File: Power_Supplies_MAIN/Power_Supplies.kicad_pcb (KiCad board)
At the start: 4 copper layers, 343.1 x 201.9 mm, 229 parts, among them IC1 PCM1865DBT, IC2 LM2940IMPX-10_NOPB, IC3 XC6902NA01PR-G, IC5 PCM1865DBT, J1 Line Out (Left), J10 XLR3_AudioJack3_Combo, J11 PINHD_1x4_Female, J13 PINHD_1x10_Female, J14 PINHD_1x10_Female, J2 Headphone Out, J20 ACJM-MV-2, J21 Line Out (Right), J29 PINHD_1x2_Female, J3 XLR3_AudioJack3_Combo, J30 PINHD_1x2_Female, J31 PINHD_1x2_Female, J32 PINHD_1x2_Female, J33 PINHD_1x3_Female, J36 PINHD_1x2_Female, J4 XLR3_AudioJack3_Combo, J5 ACJM-MV-2, J6 ACJM-MV-2, J7 ACJM-MV-2, J9 XLR3_AudioJack3_Combo, U10 OPA2134, U11 TPA6110A2DGN, U15 OPA2134, U16 SSM2019BRNZ, U17 SSM2019BRNZ, U18 OPA2134, U19 SSM2019BRNZ, U20 SSM2019BRNZ, U34 NE5532AD, U35 NE5532AD, U9 PCM1780

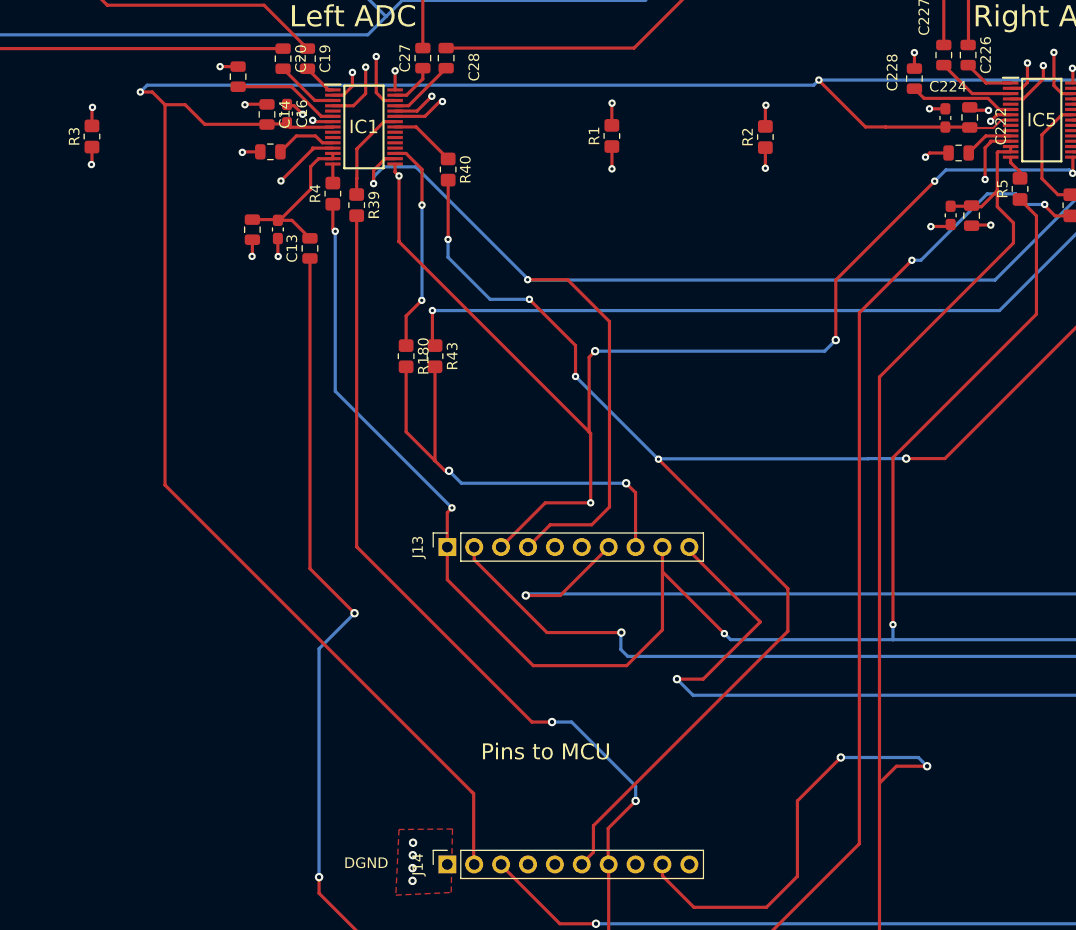
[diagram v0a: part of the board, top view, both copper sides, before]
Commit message: fixed issue w mcu getting analog voltage supply (will just use digital)
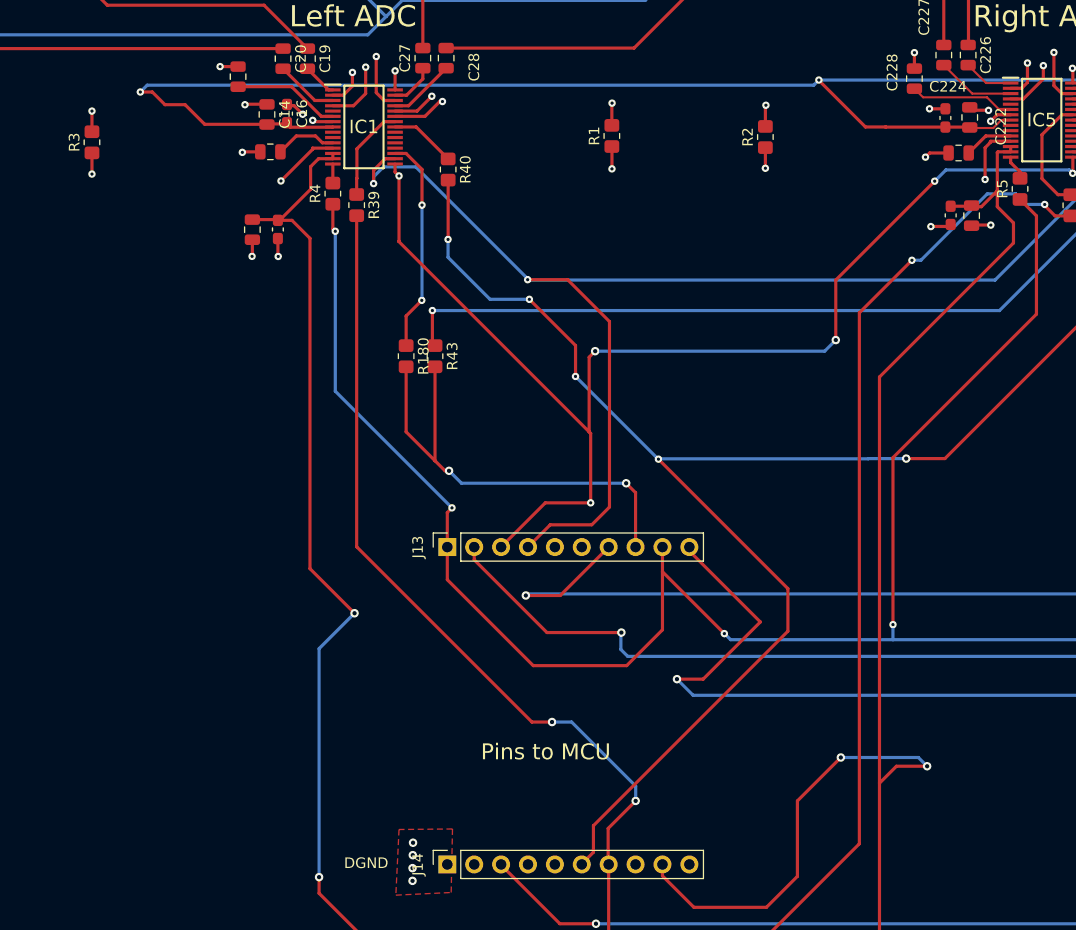
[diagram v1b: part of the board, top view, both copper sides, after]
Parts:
- removed C13: 10uF, Capacitor_SMD:C_0805_2012Metric
- moved R3 0.55 mm to (107.7, 146.1)
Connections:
- J14 pad 2: 3.3V -> unconnected-(J14-Pad2)
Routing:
- net 3.3V: track 369.3 -> 285.5 mm
- net 3.3V_2: track 249.6 -> 267.0 mm
- net Net-(IC1-DVDD): track 15.5 -> 0.00 mm

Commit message: fixed a lot of stuff
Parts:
- removed C230, C231, C27, C28, C47: 10uF, Capacitor_SMD:C_0805_2012Metric
- removed C31, C32: 1200pF, Capacitor_SMD:C_0603_1608Metric_Pad1.08x0.95mm_HandSolder
- removed C33, C35: 120pF, Capacitor_SMD:C_0603_1608Metric_Pad1.08x0.95mm_HandSolder
- removed J29, J30, J31, J36: PINHD_1x2_Female, Connector_PinSocket_2.54mm:PinSocket_1x02_P2.54mm_Vertical
- removed J33: PINHD_1x3_Female, Connector_PinSocket_2.54mm:PinSocket_1x03_P2.54mm_Vertical
- removed R180: 1k, Resistor_SMD:R_0805_2012Metric_Pad1.20x1.40mm_HandSolder
- added C1: 10uF, Capacitor_SMD:C_0805_2012Metric, F.Cu at (136.4, 136.0)
- added C2: 10uF, Capacitor_SMD:C_0805_2012Metric, F.Cu at (142.8, 137.4)
- added C3: 10uF, Capacitor_SMD:C_0805_2012Metric, F.Cu at (197.6, 134.6)
- added C4: 10uF, Capacitor_SMD:C_0805_2012Metric, F.Cu at (201.4, 136.0)
- added C5: 1uF, PCM_Capacitor_SMD_AKL:C_0805_2012Metric, F.Cu at (337.8, 205.2)
- added C6: 1uF, PCM_Capacitor_SMD_AKL:C_0805_2012Metric, F.Cu at (342.6, 202.4)
- added C7: 0.47uF, PCM_Capacitor_SMD_AKL:C_0805_2012Metric, F.Cu at (324.2, 190.6)
- added C8: 22uF, Capacitor_SMD:CP_Elec_4x5.8, F.Cu at (335.8, 190.6)
- added C9: 10uF, Capacitor_SMD:CP_Elec_4x5.8, F.Cu at (340.6, 102.2)
- added D1: LED, LED_SMD:LED_0402_1005Metric_Pad0.77x0.64mm_HandSolder, F.Cu at (183.2, 142.2)
- added D2: LED, LED_SMD:LED_0402_1005Metric_Pad0.77x0.64mm_HandSolder, F.Cu at (124.6, 151.2)
- added D3: LED, LED_SMD:LED_0402_1005Metric_Pad0.77x0.64mm_HandSolder, F.Cu at (191.5, 156.4)
- added D4: LED, LED_SMD:LED_0402_1005Metric_Pad0.77x0.64mm_HandSolder, F.Cu at (118.6, 140.8)
- added D5: LED, LED_SMD:LED_0402_1005Metric_Pad0.77x0.64mm_HandSolder, F.Cu at (319.0, 171.2)
- added D6: LED, LED_SMD:LED_0402_1005Metric_Pad0.77x0.64mm_HandSolder, F.Cu at (336.6, 94.8)
- added D7: LED, LED_SMD:LED_0402_1005Metric_Pad0.77x0.64mm_HandSolder, F.Cu at (346.8, 202.4)
- added D8: LED, LED_SMD:LED_0402_1005Metric_Pad0.77x0.64mm_HandSolder, F.Cu at (343.6, 192.8)
- added J12: PINHD_1x3_Male, Connector_PinHeader_2.54mm:PinHeader_1x03_P2.54mm_Vertical, F.Cu at (303.9, 190.0)
- added J15: PINHD_1x2_Male, Connector_PinHeader_2.54mm:PinHeader_1x02_P2.54mm_Vertical, F.Cu at (303.2, 181.0)
- added J16: PINHD_1x5_Male, Connector_PinHeader_2.54mm:PinHeader_1x05_P2.54mm_Vertical, F.Cu at (319.5, 223.0)
- added J18: PINHD_1x2_Male, Connector_PinHeader_2.54mm:PinHeader_1x02_P2.54mm_Vertical, F.Cu at (180.8, 129.3)
- added J8: PINHD_1x5_Female, Connector_PinSocket_2.54mm:PinSocket_1x05_P2.54mm_Vertical, F.Cu at (308.2, 208.2)
- added R10: 2.2k, Resistor_SMD:R_0805_2012Metric, F.Cu at (114.6, 139.4)
- added R11: 50, Resistor_SMD:R_0805_2012Metric_Pad1.20x1.40mm_HandSolder, F.Cu at (164.6, 182.8)
- added R12: 50, Resistor_SMD:R_0805_2012Metric_Pad1.20x1.40mm_HandSolder, F.Cu at (161.4, 182.0)
- added R13: 2.2k, Resistor_SMD:R_0805_2012Metric, F.Cu at (320.6, 168.0)
- added R14: 2.2k, Resistor_SMD:R_0805_2012Metric, F.Cu at (336.6, 90.7)
- added R15: 2.2k, Resistor_SMD:R_0805_2012Metric, F.Cu at (347.0, 206.0)
- added R16: 2.2k, Resistor_SMD:R_0805_2012Metric, F.Cu at (343.6, 188.4)
- added R34: 0R, Resistor_SMD:R_0805_2012Metric_Pad1.20x1.40mm_HandSolder, F.Cu at (120.4, 144.4)
- added R35: 0R, Resistor_SMD:R_0805_2012Metric_Pad1.20x1.40mm_HandSolder, F.Cu at (195.4, 150.6)
- added R36: 0R, Resistor_SMD:R_0805_2012Metric_Pad1.20x1.40mm_HandSolder, F.Cu at (175.8, 203.0)
- added R41: 50, Resistor_SMD:R_0805_2012Metric_Pad1.20x1.40mm_HandSolder, F.Cu at (173.6, 193.8)
- added R6: 2.2k, Resistor_SMD:R_0805_2012Metric, F.Cu at (181.2, 139.6)
- added R7: 2.2k, Resistor_SMD:R_0805_2012Metric, F.Cu at (120.3, 151.2)
- added R72: 2.2k, Resistor_SMD:R_0805_2012Metric_Pad1.20x1.40mm_HandSolder, F.Cu at (135.4, 193.6)
- added R73: 0R, Resistor_SMD:R_0805_2012Metric_Pad1.20x1.40mm_HandSolder, F.Cu at (177.6, 143.0)
- added R8: 0R, Resistor_SMD:R_0805_2012Metric_Pad1.20x1.40mm_HandSolder, F.Cu at (175.6, 200.4)
- added R9: 50, Resistor_SMD:R_0805_2012Metric_Pad1.20x1.40mm_HandSolder, F.Cu at (164.6, 192.8)
- added R90: 100k, PCM_Resistor_SMD_AKL:R_0402_1005Metric, F.Cu at (139.4, 134.0)
- added R91: 100k, PCM_Resistor_SMD_AKL:R_0402_1005Metric, F.Cu at (146.4, 135.8)
- added R92: 100k, PCM_Resistor_SMD_AKL:R_0402_1005Metric, F.Cu at (123.8, 131.4)
- added R93: 100k, PCM_Resistor_SMD_AKL:R_0402_1005Metric, F.Cu at (120.8, 135.7)
- added R94: 100k, PCM_Resistor_SMD_AKL:R_0402_1005Metric, F.Cu at (192.6, 133.6)
- added R95: 100k, PCM_Resistor_SMD_AKL:R_0402_1005Metric, F.Cu at (198.2, 128.1)
- added R96: 100k, PCM_Resistor_SMD_AKL:R_0402_1005Metric, F.Cu at (208.8, 135.3)
- added R97: 100k, PCM_Resistor_SMD_AKL:R_0402_1005Metric, F.Cu at (186.2, 133.6)
- added R98: 0R, Resistor_SMD:R_0805_2012Metric_Pad1.20x1.40mm_HandSolder, F.Cu at (207.0, 143.0)
- J1, J2, J21: footprint Connector_Audio:Jack_3.5mm_CUI_SJ-3523-SMT_Horizontal -> SamacSys_Parts:ACJSNV353
- J10, J3, J4, J9: footprint Connector_Audio:Jack_XLR-6.35mm_Neutrik_NCJ6FA-H_Horizontal -> Connector_Audio:Jack_XLR-6.35mm_Neutrik_NCJ6FA-V_Vertical
- J11: value PINHD_1x4_Female -> PINHD_1x1_Male; footprint Connector_PinSocket_2.54mm:PinSocket_1x04_P2.54mm_Vertical -> Connector_PinHeader_2.54mm:PinHeader_1x01_P2.54mm_Vertical
- R19, R21, R22: value 100 -> 50
- R20: value 100 -> 0R
- R37, R38, R39, R40: value 1k -> 0R
- R4: value 1k -> 0
- R42: value 5k -> 0R; footprint Resistor_SMD:R_0603_1608Metric_Pad0.98x0.95mm_HandSolder -> Resistor_SMD:R_0805_2012Metric_Pad1.20x1.40mm_HandSolder
- R43: value 1k -> 2.2k
- R5: value 1k -> 2.2k; footprint Resistor_SMD:R_0805_2012Metric_Pad1.20x1.40mm_HandSolder -> Resistor_SMD:R_0805_2012Metric
- moved J11 216.2 mm to (94.7, 204.9)
- moved R42 72.5 mm to (175.8, 208.0), turned to 180 degrees
- moved J3 34.2 mm to (60.1, 61.7), turned to 0 degrees
- moved J14 29.1 mm to (139.4, 185.2), turned to 0 degrees
- moved J13 28.2 mm to (169.4, 185.2), turned to 0 degrees
- moved R43 28.2 mm to (133.0, 193.6), turned to 90 degrees
- moved J9 27.8 mm to (90.1, 61.7), turned to 0 degrees
- moved J4 23.9 mm to (120.1, 61.7), turned to 0 degrees
- moved J10 23.8 mm to (150.1, 61.7), turned to 0 degrees
- moved J20 16.3 mm to (214.8, 65.7)
- moved J5 16.3 mm to (194.8, 65.7)
- moved J6 16.3 mm to (234.8, 65.7)
- moved J7 16.3 mm to (254.8, 65.7)
- moved J1 13.7 mm to (281.2, 65.7)
- moved R5 10.9 mm to (188.2, 158.7), turned to -90 degrees
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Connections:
- C14 pad 2: 3.3V -> Net-(IC1-AVDD)
- C16 pad 2: 3.3V -> Net-(IC1-AVDD)
- C19 pad 2: Net-(IC1-VINL2/VIN1M) -> Net-(IC1-VINR1/VIN2P)
- C222 pad 2: 3.3V -> Net-(IC5-AVDD)
- C224 pad 2: 3.3V -> Net-(IC5-AVDD)
- C226 pad 2: Net-(IC5-VINL2/VIN1M) -> Net-(IC5-VINR1/VIN2P)
- IC1 pad 18: Net-(IC1-DOUT) -> DIN
- IC1 pad 2: AGND -> Net-(IC1-VINR2/VIN2M)
- IC1 pad 27: Net-(IC1-VINL4/VIN4M) -> unconnected-(IC1-VINL4/VIN4M-Pad27)
- IC1 pad 28: AGND -> unconnected-(IC1-VINR4/VIN3M-Pad28)
- IC1 pad 29: Net-(IC1-VINL3/VIN4P) -> unconnected-(IC1-VINL3/VIN4P-Pad29)
- IC1 pad 30: AGND -> unconnected-(IC1-VINR3/VIN3P-Pad30)
- IC1 pad 4: AGND -> Net-(IC1-VINR1/VIN2P)
- IC1 pad 8: 3.3V -> Net-(IC1-AVDD)
- IC3 pad 4: AGND -> REAL_-12V
- IC5 pad 18: Net-(IC5-DOUT) -> DIN
- IC5 pad 2: AGND -> Net-(IC5-VINR2/VIN2M)
- IC5 pad 27: Net-(IC5-VINL4/VIN4M) -> unconnected-(IC5-VINL4/VIN4M-Pad27)
- IC5 pad 28: AGND -> unconnected-(IC5-VINR4/VIN3M-Pad28)
- IC5 pad 29: Net-(IC5-VINL3/VIN4P) -> unconnected-(IC5-VINL3/VIN4P-Pad29)
- IC5 pad 30: AGND -> unconnected-(IC5-VINR3/VIN3P-Pad30)
- IC5 pad 4: AGND -> Net-(IC5-VINR1/VIN2P)
- IC5 pad 8: 3.3V -> Net-(IC5-AVDD)
- J11 pad 1: 3.3V -> 3.3V_2
- J13 pad 10: BCLK_DAC -> Net-(J13-Pad10)
- J13 pad 2: DATA -> Net-(J13-Pad2)
- J13 pad 3: LRCK_ADC -> Net-(J13-Pad3)
- J13 pad 4: BCLK_ADC -> Net-(J13-Pad4)
- J13 pad 7: LRCK_DAC -> Net-(J13-Pad7)
- J13 pad 8: DIN -> Net-(J13-Pad8)
- J13 pad 9: MCLK -> Net-(J13-Pad9)
- J14 pad 3: 5V -> 3.3V_2
- R42 pad 1: Net-(IC5-MS/AD) -> BCLK_DAC
- R42 pad 2: 3.3V -> Net-(J13-Pad10)
- R43 pad 1: Net-(IC5-DOUT) -> SCL
- R43 pad 2: DIN -> 3.3V_2
- R5 pad 1: MCLK -> Net-(D3-Pad1)
- R5 pad 2: Net-(IC5-SCKI) -> DGND
- R54 pad 2: Net-(J29-Pad2) -> 36V
- R56 pad 2: Net-(J30-Pad2) -> 36V
- R82 pad 2: Net-(J31-Pad2) -> 36V
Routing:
- net 36V: track 0.00 -> 179.3 mm, vias 0 -> 6
- net 5V: track 312.5 -> 204.5 mm, vias 7 -> 4
- net DIN: track 44.2 -> 135.0 mm, vias 2 -> 3
- net Net-(IC5-DOUT): track 80.4 -> 0.00 mm, vias 2 -> 0
- net Net-(C102-Pad1): track 48.7 -> 108.2 mm, vias 3 -> 5
- net Net-(C91-Pad2): track 5.02 -> 59.6 mm, vias 0 -> 2
- net Net-(C63-Pad2): track 44.5 -> 95.4 mm, vias 3 -> 5
- net Net-(C60-Pad2): track 6.86 -> 56.5 mm
- net Net-(C61-Pad2): track 6.57 -> 55.2 mm, vias 0 -> 2
- net SCL: track 185.7 -> 140.7 mm, vias 4 -> 6
- net Net-(C100-Pad1): track 44.9 -> 88.7 mm, vias 3 -> 5
- net Net-(C54-Pad2): track 17.1 -> 58.3 mm, vias 0 -> 2
- net Net-(C103-Pad1): track 17.8 -> 57.8 mm
- net 3.3V_2: track 267.0 -> 227.3 mm, vias 4 -> 2
- net Net-(C101-Pad1): track 15.0 -> 53.2 mm, vias 0 -> 2
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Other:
- board text added: "3.3V (Digital)"
- board text added: "30mm Apart"
- board text added: "5V"
- board text added: "Test Point"
- board text added: "V2 :("
- board text removed: "40mm Apart"
- board text removed: "V1"

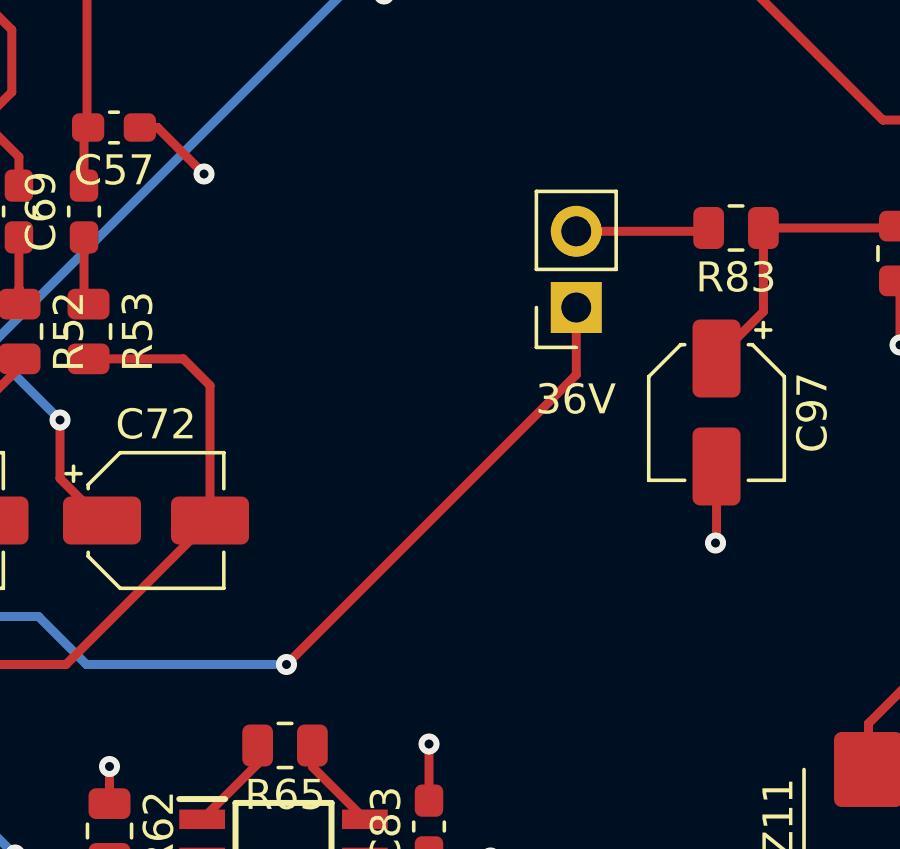
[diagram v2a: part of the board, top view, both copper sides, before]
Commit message: fixed power board problems/...
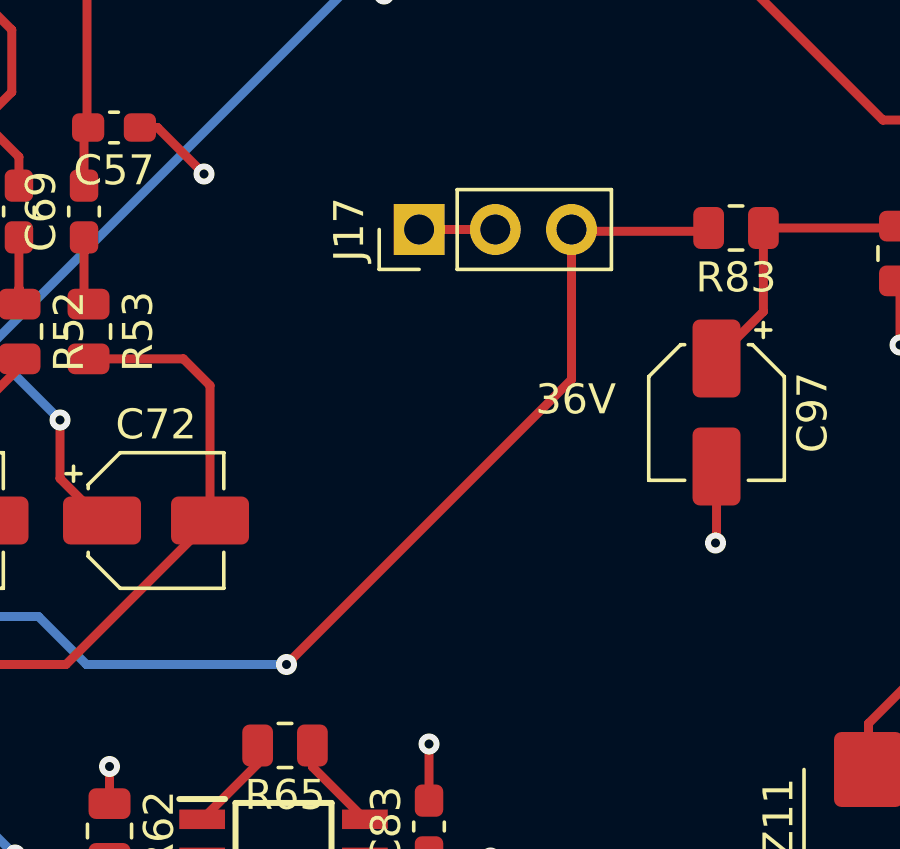
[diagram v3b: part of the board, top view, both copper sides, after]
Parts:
- removed J32: PINHD_1x2_Female, Connector_PinSocket_2.54mm:PinSocket_1x02_P2.54mm_Vertical
- added J17: PINHD_1x3_Male, Connector_PinHeader_2.54mm:PinHeader_1x03_P2.54mm_Vertical, F.Cu at (138.4, 96.1)
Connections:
- R83 pad 2: Net-(J32-Pad2) -> 36V
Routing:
- net 36V: track 179.3 -> 186.3 mm
- net Net-(J32-Pad2): track 4.46 -> 0.00 mm
- net 36V_INPUT: track 0.00 -> 2.54 mm

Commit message: made new pcbs :(
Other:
- board size 343.1 x 201.9 mm -> 327.6 x 186.9 mm
- board text removed: "L"
- board text removed: "R"
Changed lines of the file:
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@@
 		)
 		(fp_text user "${REFERENCE}"
-			(at 0 2.54 360)
+			(at 0 2.54 0)
 			(layer "F.Fab")
 			(effects
@@
 	)
 	(gr_rect
-		(start 16.5 34.45)
-		(end 359.6 236.4)
+		(start 25.1 42.6)
+		(end 352.7 229.5)
 		(stroke
 			(width 0.05)
@@
 		(layer "Edge.Cuts")
 	)
-	(gr_text "R"
-		(at 23.7 193.425 90)
-		(layer "F.SilkS")
-		(effects
-			(font
-				(size 1 1)
-				(thickness 0.1)
-			)
-			(justify left bottom)
-		)
-	)
 	(gr_text "-12V"
 		(at 314.4 216.2 0)
@@
 		)
 	)
-	(gr_text "L"
-		(at 23.25 207.9 90)
-		(layer "F.SilkS")
-		(effects
-			(font
-				(size 1 1)
-				(thickness 0.1)
-			)
-			(justify left bottom)
-		)
-	)
